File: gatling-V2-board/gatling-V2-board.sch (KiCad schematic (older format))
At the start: 34 parts, among them IC2 TRANSCEIVER_CAN_33, J1 645002114822, J10 61900311121, J11 61900311121, J12 61900311121, J13 61900311121, J2 62000411622, J3 61900311121, J4 61900311121, J5 691311700102, J6 Conn_01x04_Male, J7 653006114822, J9 62000411622, U1 Teensy3.2

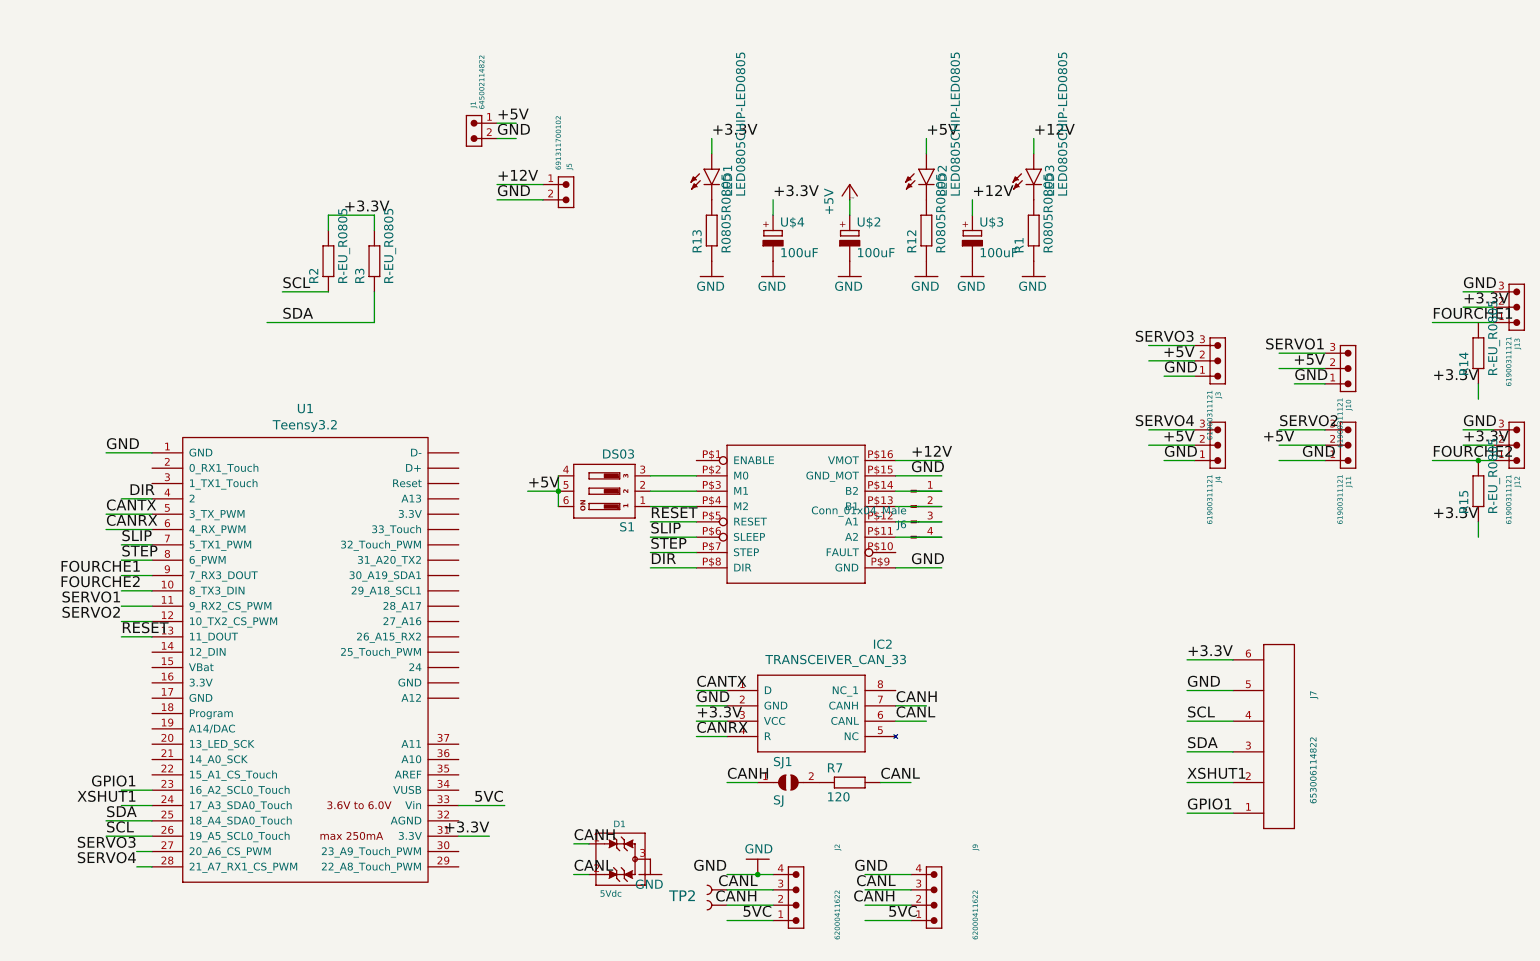
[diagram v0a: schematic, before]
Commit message: Lib composant créée+pcb gatling mises à jours avec teensy (a verifier avant prod)
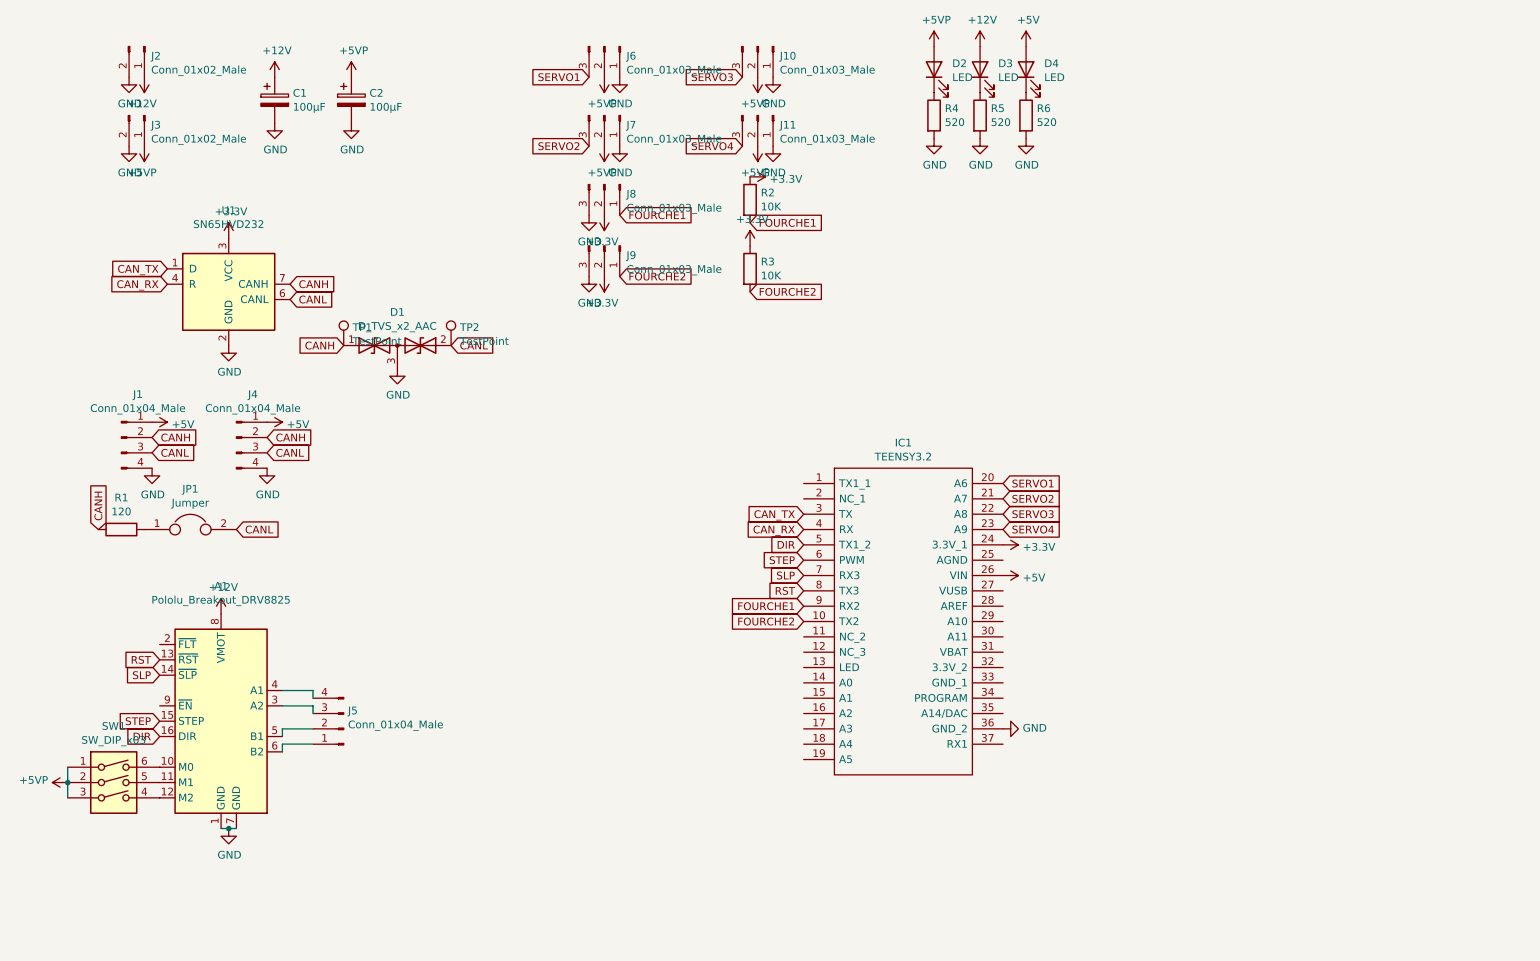
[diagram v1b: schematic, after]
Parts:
- removed D1: 5Vdc, schematic prebarillet:WE-TVS_SOT23-3L, symbol schematic_prebarillet-eagle-import:WE-TVS_SOT23-3L_824022
- removed IC2: TRANSCEIVER_CAN_33, schematic prebarillet:SOIC127P600X175-8N, symbol schematic_prebarillet-eagle-import:TRANSCEIVER_CAN_33
- removed J1: 645002114822, schematic prebarillet:645002114822, symbol schematic_prebarillet-eagle-import:645002114822
- removed J10, J11, J12, J13, J3, J4: 61900311121, schematic prebarillet:61900311121, symbol schematic_prebarillet-eagle-import:61900311121
- removed J2, J9: 62000411622, schematic prebarillet:62000411622, symbol schematic_prebarillet-eagle-import:62000411622
- removed J5: 691311700102, schematic prebarillet:691311700102, symbol schematic_prebarillet-eagle-import:691311700102
- removed J6: Conn_01x04_Male, Connector_PinHeader_2.54mm:PinHeader_1x04_P2.54mm_Horizontal, symbol Connector:Conn_01x04_Male
- removed J7: 653006114822, schematic prebarillet:653006114822, symbol schematic_prebarillet-eagle-import:653006114822
- removed LED1, LED2, LED3: LED0805CHIP-LED0805, LED_SMD:LED_0805_2012Metric_Pad1.15x1.40mm_HandSolder, symbol schematic_prebarillet-eagle-import:LED0805CHIP-LED0805
- removed R1, R12, R13: R0805R0805, Resistor_SMD:R_0805_2012Metric_Pad1.15x1.40mm_HandSolder, symbol schematic_prebarillet-eagle-import:R0805R0805
- removed R14, R15, R2, R3: R-EU_R0805, Resistor_SMD:R_0805_2012Metric_Pad1.15x1.40mm_HandSolder, symbol schematic_prebarillet-eagle-import:R-EU_R0805
- removed R7: 120, Resistor_SMD:R_0805_2012Metric_Pad1.15x1.40mm_HandSolder, symbol schematic_prebarillet-eagle-import:R-EU_R0805
- removed S1: DS03, schematic prebarillet:DS-03, symbol schematic_prebarillet-eagle-import:DS03
- removed SJ1: SJ, Connector_PinHeader_2.54mm:PinHeader_1x02_P2.54mm_Vertical, symbol schematic_prebarillet-eagle-import:SJ
- removed TP1, TP2: TEST-POINT3X5, schematic prebarillet:PAD.03X.05, symbol schematic_prebarillet-eagle-import:TEST-POINT3X5
- removed U$1: DRV8825, schematic prebarillet:DRV8825, symbol schematic_prebarillet-eagle-import:DRV8825
- removed U$2, U$3, U$4: 100uF, schematic prebarillet:E2-5, symbol schematic_prebarillet-eagle-import:CONDO2-5
- removed U1: Teensy3.2, teensy:Teensy30_31_32_LC, symbol teensy:Teensy3.2
- added A1: Pololu_Breakout_DRV8825, Module:Pololu_Breakout-16_15.2x20.3mm, symbol Driver_Motor:Pololu_Breakout_DRV8825
- added C1, C2: 100µF, Capacitor_THT:CP_Radial_D8.0mm_P3.50mm, symbol Device:CP
- added D1: D_TVS_x2_AAC, Package_TO_SOT_SMD:SOT-23, symbol Device:D_TVS_x2_AAC
- added D2, D3, D4: LED, LED_SMD:LED_0805_2012Metric, symbol Device:LED
- added IC1: TEENSY3.2, AREA_lib_composant:TEENSY32, symbol AREA_composant:TEENSY3.2
- added J1, J4: Conn_01x04_Male, AREA_lib_Connector:Wuerth_2mm_4pin_62000411622, symbol Connector:Conn_01x04_Male
- added J10, J11, J6, J7, J8, J9: Conn_01x03_Male, AREA_lib_Connector:Wuerth_2.54mm_3pins_61900311121, symbol Connector:Conn_01x03_Male
- added J2, J3: Conn_01x02_Male, AREA_lib_Connector:Wuerth_3.96mm_2pin_645002114822, symbol Connector:Conn_01x02_Male
- added J5: Conn_01x04_Male, Connector_PinHeader_2.54mm:PinHeader_1x04_P2.54mm_Horizontal, symbol Connector:Conn_01x04_Male
- added JP1: Jumper, Connector_PinHeader_2.54mm:PinHeader_1x02_P2.54mm_Vertical, symbol Device:Jumper
- added R1: 120, Resistor_SMD:R_0603_1608Metric, symbol Device:R
- added R2, R3: 10K, Resistor_SMD:R_0603_1608Metric, symbol Device:R
- added R4, R5, R6: 520, Resistor_SMD:R_0603_1608Metric, symbol Device:R
- added SW1: SW_DIP_x03, Button_Switch_SMD:SW_DIP_SPSTx03_Slide_6.7x9.18mm_W6.73mm_P2.54mm_LowProfile_JPin, symbol Switch:SW_DIP_x03
- added TP1, TP2: TestPoint, TestPoint:TestPoint_Keystone_5000-5004_Miniature, symbol Connector:TestPoint
- added U1: SN65HVD232, Package_SO:SOIC-8_3.9x4.9mm_P1.27mm, symbol Interface_CAN_LIN:SN65HVD232
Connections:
- net labels added: +5VP, CAN_RX, CAN_TX, RST, SLP
- net labels removed: 5VC, CANRX, CANTX, GPIO1, RESET, SCL, SDA, SLIP, XSHUT1
- wire segments 98 -> 12
